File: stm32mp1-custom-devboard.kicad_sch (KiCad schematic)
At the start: 26 parts, among them CON6 TC2050-IDC-NL-SWI, P1 Main Power Supply, Sw1 434153017835, Sw2 434153017835, U10 APX803D-29SRG-7, U11 IP4220CZ6

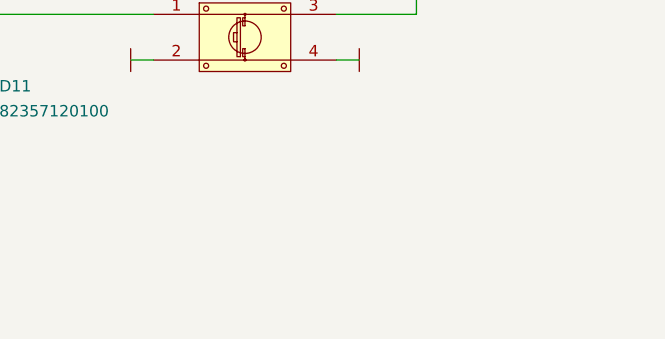
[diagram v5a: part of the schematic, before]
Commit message: Eliminated all warnings realted with footprints
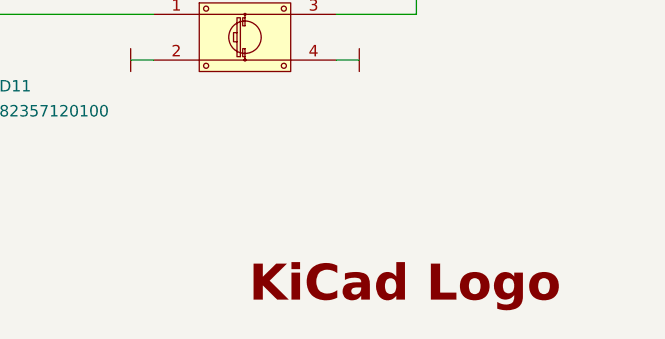
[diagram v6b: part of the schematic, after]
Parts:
- added REF1: KiCad_Logo, Symbols:KiCad-Logo2_12mm_SilkScreen, symbol Symbols:KiCad_Logo
- C54: footprint Capacitors_Smd_0603:100nF_0603 -> Capacitors_Smd_0402:100nF_0402; symbol Capacitors_Smd0603:100n -> Capacitors_Smd0402:100nF; Developer (none) -> MW; LCSC Part # (optional) (none) -> C131394; Manufacturer SAMSUNG -> Murata; Manufacturer Part Number CL10B104JB8NNNC -> GRM155R71H104KE14D; Package 0603 -> 0402; Package_1 (none) -> 0402; Price@1000pcs 0,02231 -> 0,03299; Price@1pc 0,04540 -> 0,07091; Supplier TME -> Tme; Supplier Part Number CL10B104JB8NNNC -> GRM155R71H104KE14D; URL https://www.tme.eu/pl/details/cl10b104jb8nnnc/kondensatory-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 -> https://www.tme.eu/pl/details/grm155r71h104ke14d/kondensato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
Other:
- company: Embedded System Labs -> Sofjan

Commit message: Gerbers created, BOM, CPL
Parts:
- C54: value 100n -> 100nF/50V

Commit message: New branch created
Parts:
- added R79: (no value), symbol Resistors_Smd0402:0R
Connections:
- net 3V3: now also R58.1, R59.1
- net GND: no longer R58.1, R59.1
- net STLink Module/JTRST: now also R79.1
- net STM32MP1 module/STM32-~{RST} renamed STM32-~{RST}
- net STM32-~{RST}: now also R79.2
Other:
- moved on the sheet: R58, R59
